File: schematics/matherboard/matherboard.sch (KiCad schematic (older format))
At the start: 27 parts, among them J1 RJ12, J2 RJ12, P1 VCC/GND, P2 CONN_01X05, P3 USB_B, P4 CONN_01X05, U1 FT232RL, U3 STAB3.3, U4 ESP8266, U5 Arduino_Mini

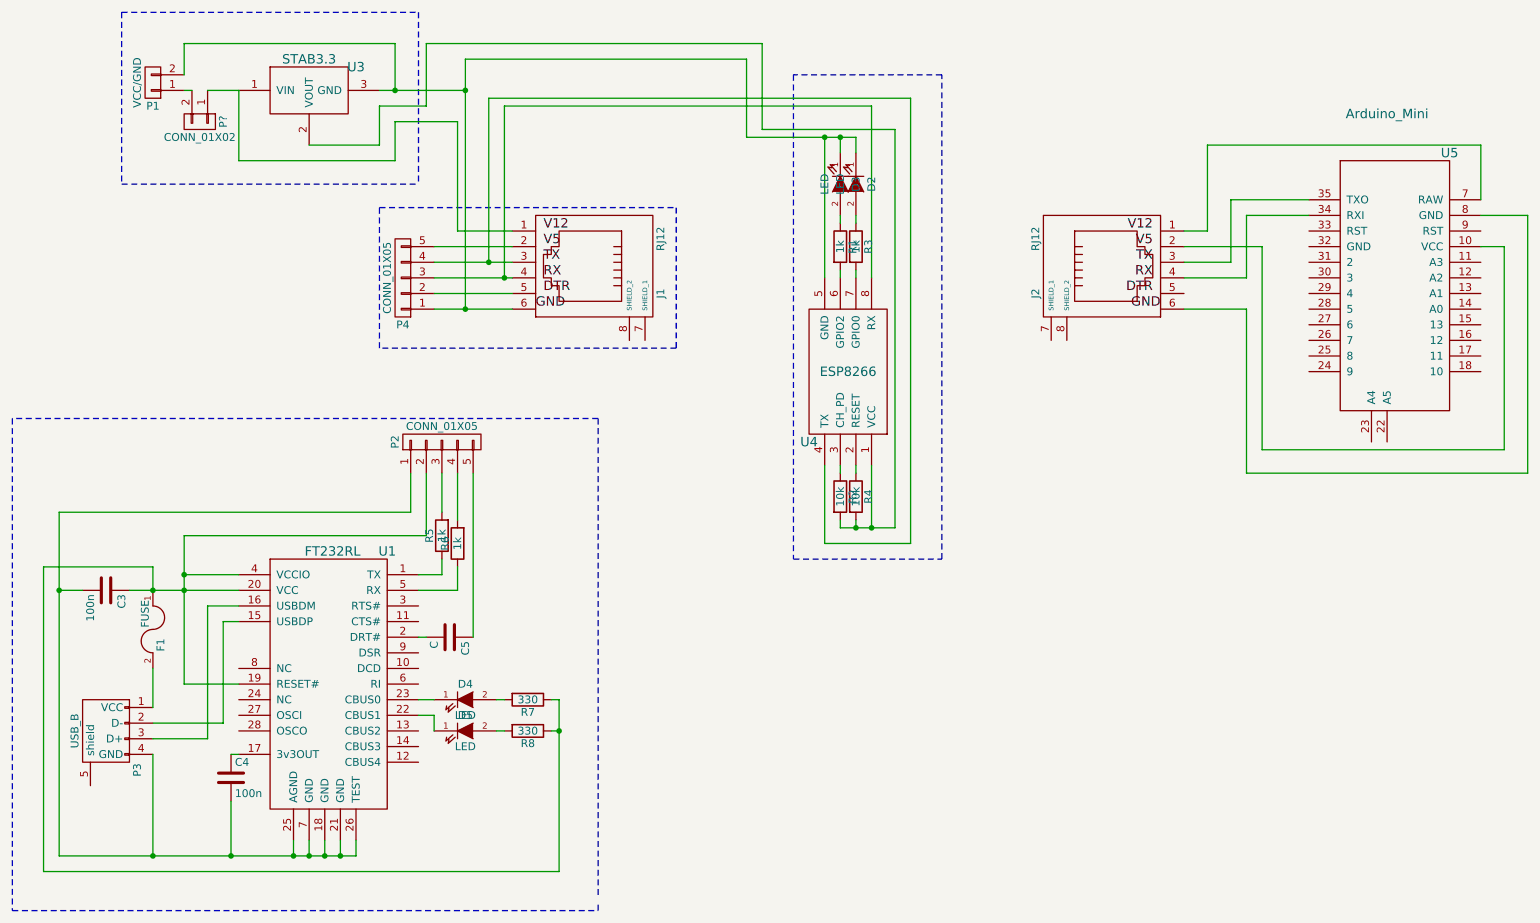
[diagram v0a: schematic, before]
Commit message: Remove USBtoTTL from matherboard
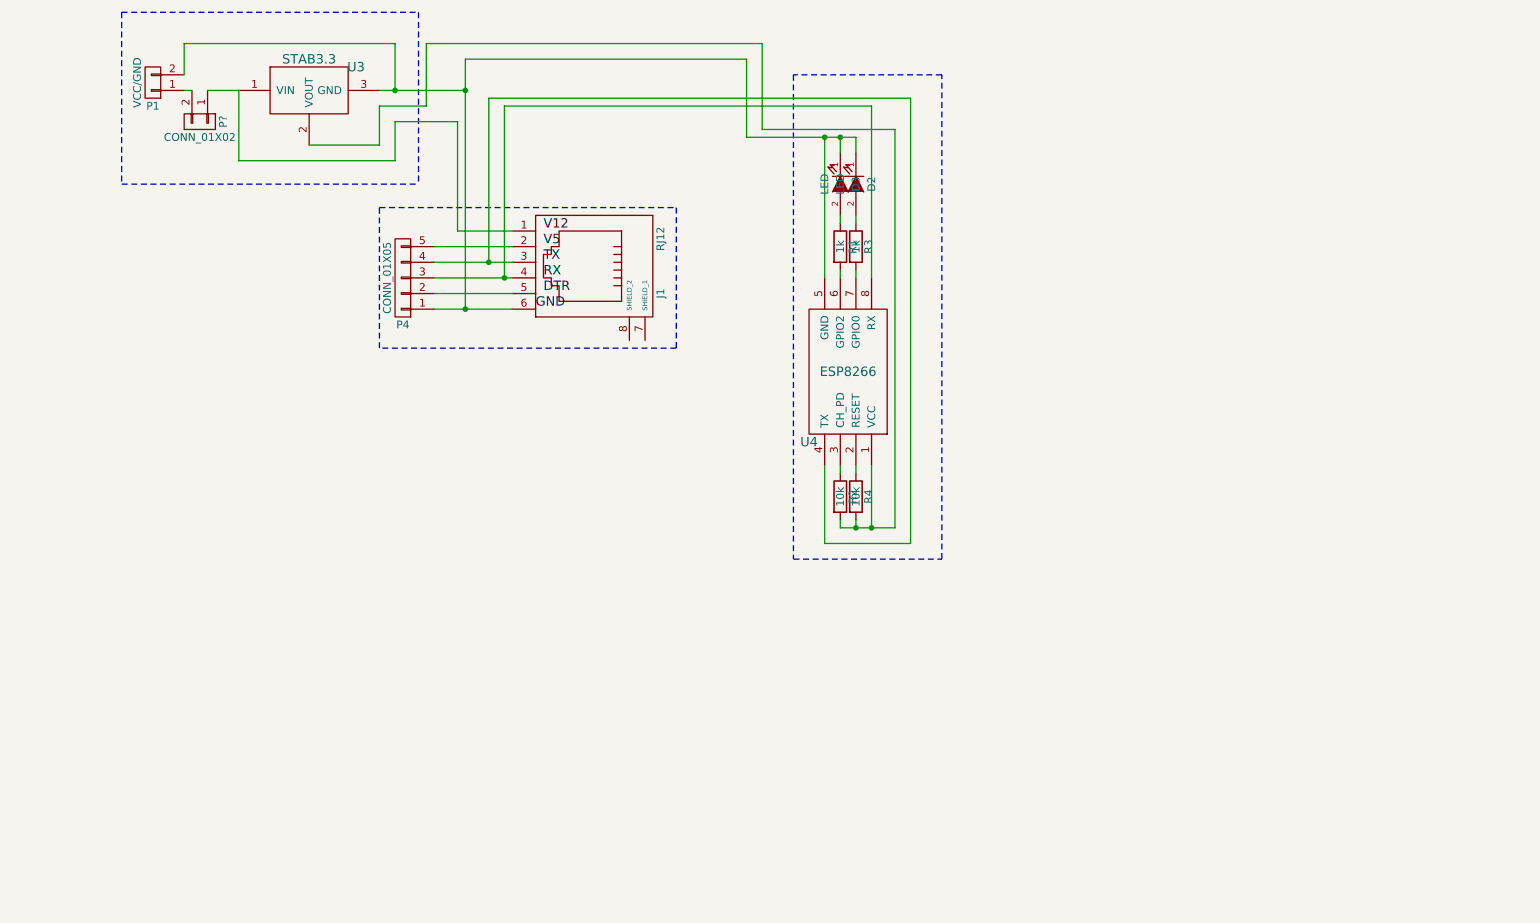
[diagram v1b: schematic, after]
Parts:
- removed C3, C4: 100n, Capacitors_ThroughHole:C_Rect_L4_W2.5_P2.5, symbol C
- removed C5: C, Capacitors_ThroughHole:C_Rect_L4_W2.5_P2.5, symbol C
- removed D4, D5: LED, LEDs:LED-3MM, symbol LED
- removed F1: FUSE, w_pth_resistors:RC05, symbol FUSE
- removed J2: RJ12, Connect:RJ12_E, symbol RJ12
- removed P2: CONN_01X05, Pin_Headers:Pin_Header_Straight_1x05, symbol CONN_01X05
- removed P3: USB_B, Connect:USB_B, symbol USB_B
- removed R5, R6: 1k, Resistors_ThroughHole:Resistor_Horizontal_RM7mm, symbol R
- removed R7, R8: 330, Resistors_ThroughHole:Resistor_Horizontal_RM7mm, symbol R
- removed U1: FT232RL, Housings_SSOP:SSOP-28_5.3x10.2mm_Pitch0.65mm, symbol FT232RL
- removed U5: Arduino_Mini, symbol Arduino_Mini
